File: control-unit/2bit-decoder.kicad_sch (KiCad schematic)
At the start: 0 parts

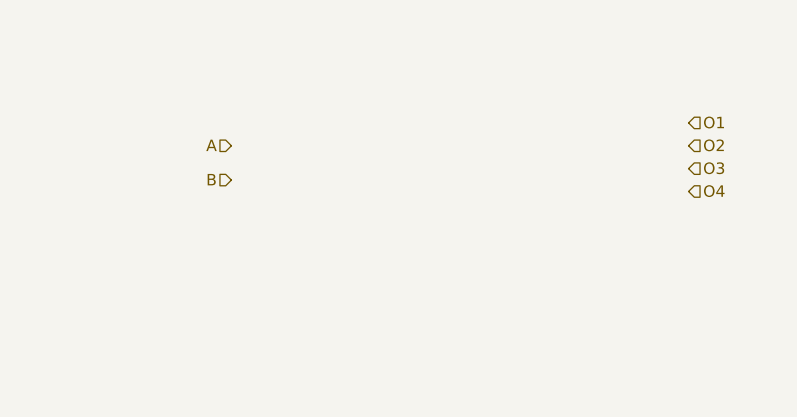
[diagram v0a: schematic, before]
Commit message: complete 2-bit encoder
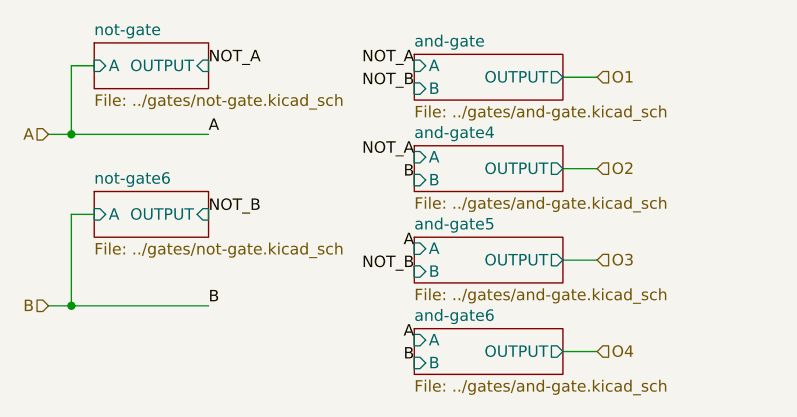
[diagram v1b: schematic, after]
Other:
- added sheet and-gate (../gates/and-gate.kicad_sch)
- added sheet and-gate4 (../gates/and-gate.kicad_sch)
- added sheet and-gate5 (../gates/and-gate.kicad_sch)
- added sheet and-gate6 (../gates/and-gate.kicad_sch)
- added sheet not-gate (../gates/not-gate.kicad_sch)
- added sheet not-gate6 (../gates/not-gate.kicad_sch)
